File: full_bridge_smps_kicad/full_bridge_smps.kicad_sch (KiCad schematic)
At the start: 0 parts

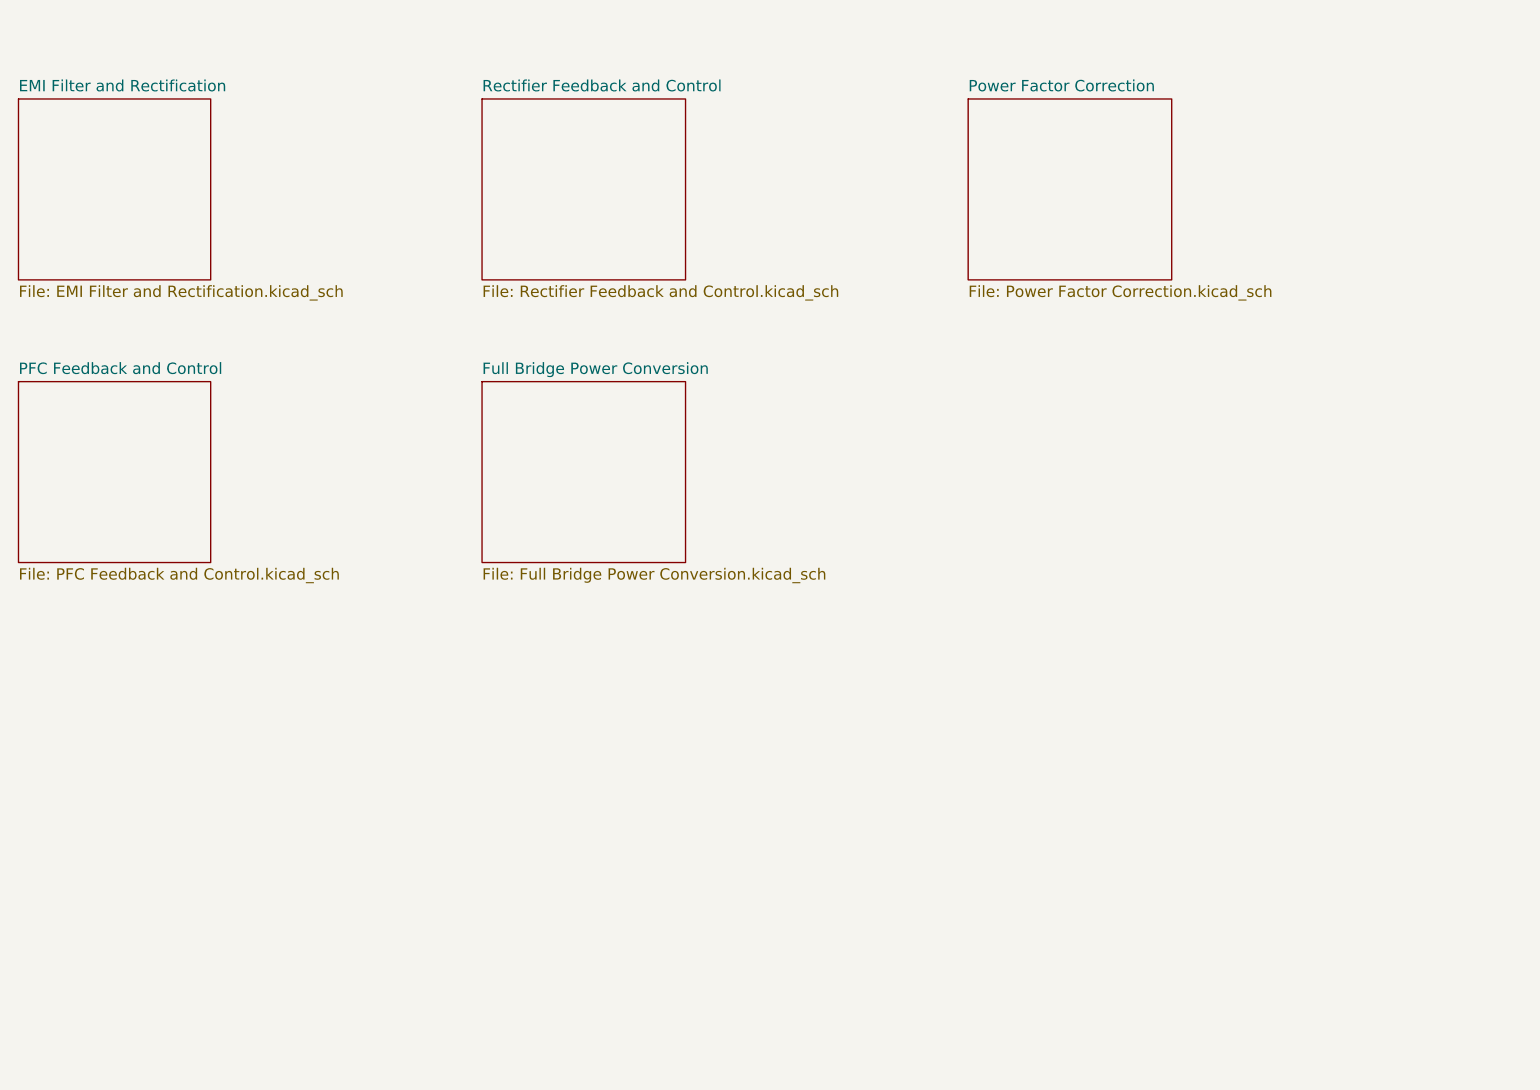
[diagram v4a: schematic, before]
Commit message: Finishing up the output rectification, creating new pages for the corresponding feedback and drive circuits
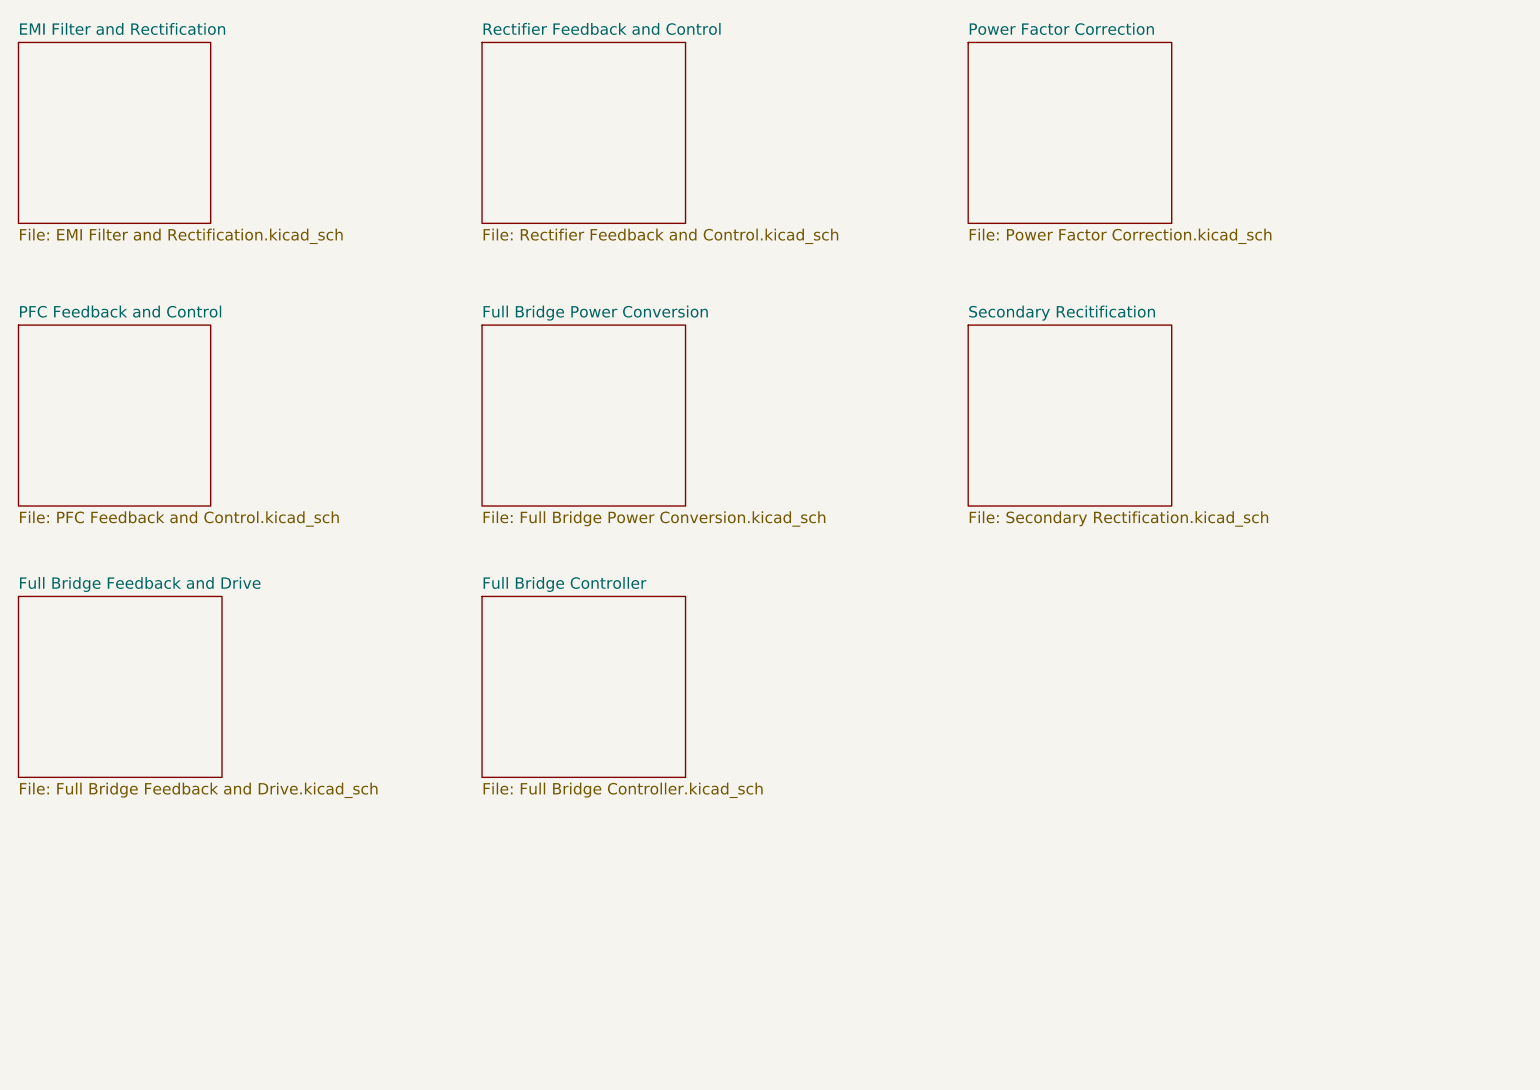
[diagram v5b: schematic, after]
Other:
- added sheet Full Bridge Controller (Full Bridge Controller.kicad_sch)
- added sheet Full Bridge Feedback and Drive (Full Bridge Feedback and Drive.kicad_sch)
- added sheet Secondary Recitification (Secondary Rectification.kicad_sch)
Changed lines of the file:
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@@
     (rev "1.0.0")
   )
-  (sheet (at 24.13 22.86) (size 21.59 20.32) (fields_autoplaced)
+  (sheet (at 24.13 16.51) (size 21.59 20.32) (fields_autoplaced)
     (stroke (width 0.1524) (type solid))
     (fill (color 0 0 0 0.0000))
-    (property "Sheetname" "EMI Filter and Rectification" (at 24.13 22.1484 0)
+    (property "Sheetname" "EMI Filter and Rectification" (at 24.13 15.7984 0)
       (effects (font (size 1.27 1.27)) (justify left bottom))
     )
-    (property "Sheetfile" "EMI Filter and Rectification.kicad_sch" (at 24.13 43.7646 0)
+    (property "Sheetfile" "EMI Filter and Rectification.kicad_sch" (at 24.13 37.4146 0)
       (effects (font (size 1.27 1.27)) (justify left top))
     )
@@
     )
   )
-  (sheet (at 76.2 54.61) (size 22.86 20.32) (fields_autoplaced)
+  (sheet (at 24.13 78.74) (size 22.86 20.32) (fields_autoplaced)
     (stroke (width 0.1524) (type solid))
     (fill (color 0 0 0 0.0000))
-    (property "Sheetname" "Full Bridge Power Conversion" (at 76.2 53.8984 0)
+    (property "Sheetname" "Full Bridge Feedback and Drive" (at 24.13 78.0284 0)
       (effects (font (size 1.27 1.27)) (justify left bottom))
     )
-    (property "Sheetfile" "Full Bridge Power Conversion.kicad_sch" (at 76.2 75.5146 0)
+    (property "Sheetfile" "Full Bridge Feedback and Drive.kicad_sch" (at 24.13 99.6446 0)
+      (effects (font (size 1.27 1.27)) (justify left top))
+    )
+    (instances
+      (project "full_bridge_smps"
+        (path "/f89200e7-8fc9-4acb-bb2b-7da3a53d52f5" (page "8"))
+      )
+    )
+  )
+  (sheet (at 76.2 48.26) (size 22.86 20.32) (fields_autoplaced)
+    (stroke (width 0.1524) (type solid))
+    (fill (color 0 0 0 0.0000))
+    (property "Sheetname" "Full Bridge Power Conversion" (at 76.2 47.5484 0)
+      (effects (font (size 1.27 1.27)) (justify left bottom))
+    )
+    (property "Sheetfile" "Full Bridge Power Conversion.kicad_sch" (at 76.2 69.1646 0)
       (effects (font (size 1.27 1.27)) (justify left top))
     )
@@
     )
   )
-  (sheet (at 130.81 22.86) (size 22.86 20.32) (fields_autoplaced)
+  (sheet (at 76.2 78.74) (size 22.86 20.32) (fields_autoplaced)
     (stroke (width 0.1524) (type solid))
     (fill (color 0 0 0 0.0000))
-    (property "Sheetname" "Power Factor Correction" (at 130.81 22.1484 0)
+    (property "Sheetname" "Full Bridge Controller" (at 76.2 78.0284 0)
       (effects (font (size 1.27 1.27)) (justify left bottom))
     )
-    (property "Sheetfile" "Power Factor Correction.kicad_sch" (at 130.81 43.7646 0)
+    (property "Sheetfile" "Full Bridge Controller.kicad_sch" (at 76.2 99.6446 0)
+      (effects (font (size 1.27 1.27)) (justify left top))
+    )
+    (instances
+      (project "full_bridge_smps"
+        (path "/f89200e7-8fc9-4acb-bb2b-7da3a53d52f5" (page "9"))
+      )
+    )
+  )
+  (sheet (at 130.81 48.26) (size 22.86 20.32) (fields_autoplaced)
+    (stroke (width 0.1524) (type solid))
+    (fill (color 0 0 0 0.0000))
+    (property "Sheetname" "Secondary Recitification" (at 130.81 47.5484 0)
+      (effects (font (size 1.27 1.27)) (justify left bottom))
+    )
+    (property "Sheetfile" "Secondary Rectification.kicad_sch" (at 130.81 69.1646 0)
+      (effects (font (size 1.27 1.27)) (justify left top))
+    )
+    (instances
+      (project "full_bridge_smps"
+        (path "/f89200e7-8fc9-4acb-bb2b-7da3a53d52f5" (page "7"))
+      )
+    )
+  )
+  (sheet (at 130.81 16.51) (size 22.86 20.32) (fields_autoplaced)
+    (stroke (width 0.1524) (type solid))
+    (fill (color 0 0 0 0.0000))
+    (property "Sheetname" "Power Factor Correction" (at 130.81 15.7984 0)
+      (effects (font (size 1.27 1.27)) (justify left bottom))
+    )
+    (property "Sheetfile" "Power Factor Correction.kicad_sch" (at 130.81 37.4146 0)
       (effects (font (size 1.27 1.27)) (justify left top))
     )
@@
     )
   )
-  (sheet (at 76.2 22.86) (size 22.86 20.32) (fields_autoplaced)
+  (sheet (at 76.2 16.51) (size 22.86 20.32) (fields_autoplaced)
     (stroke (width 0.1524) (type solid))
     (fill (color 0 0 0 0.0000))
-    (property "Sheetname" "Rectifier Feedback and Control" (at 76.2 22.1484 0)
+    (property "Sheetname" "Rectifier Feedback and Control" (at 76.2 15.7984 0)
       (effects (font (size 1.27 1.27)) (justify left bottom))
     )
-    (property "Sheetfile" "Rectifier Feedback and Control.kicad_sch" (at 76.2 43.7646 0)
+    (property "Sheetfile" "Rectifier Feedback and Control.kicad_sch" (at 76.2 37.4146 0)
       (effects (font (size 1.27 1.27)) (justify left top))
     )
@@
     )
   )
-  (sheet (at 24.13 54.61) (size 21.59 20.32) (fields_autoplaced)
+  (sheet (at 24.13 48.26) (size 21.59 20.32) (fields_autoplaced)
     (stroke (width 0.1524) (type solid))
     (fill (color 0 0 0 0.0000))
-    (property "Sheetname" "PFC Feedback and Control" (at 24.13 53.8984 0)
+    (property "Sheetname" "PFC Feedback and Control" (at 24.13 47.5484 0)
       (effects (font (size 1.27 1.27)) (justify left bottom))
     )
-    (property "Sheetfile" "PFC Feedback and Control.kicad_sch" (at 24.13 75.5146 0)
+    (property "Sheetfile" "PFC Feedback and Control.kicad_sch" (at 24.13 69.1646 0)
       (effects (font (size 1.27 1.27)) (justify left top))
     )

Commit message: A bit of refactoring, saving work for the day
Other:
- removed sheet Full Bridge Feedback and Drive
- added sheet Full Bridge Current Feedback and Drive (Full Bridge Current Feedback and Drive.kicad_sch)
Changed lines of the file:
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@@
     (rev "1.0.0")
+  )
+  (sheet (at 24.13 77.47) (size 22.86 20.32) (fields_autoplaced)
+    (stroke (width 0.1524) (type solid))
+    (fill (color 0 0 0 0.0000))
+    (property "Sheetname" "Full Bridge Current Feedback and Drive" (at 24.13 76.7584 0)
+      (effects (font (size 1.27 1.27)) (justify left bottom))
+    )
+    (property "Sheetfile" "Full Bridge Current Feedback and Drive.kicad_sch" (at 24.13 98.3746 0)
+      (effects (font (size 1.27 1.27)) (justify left top))
+    )
+    (instances
+      (project "full_bridge_smps"
+        (path "/f89200e7-8fc9-4acb-bb2b-7da3a53d52f5" (page "8"))
+      )
+    )
   )
   (sheet (at 24.13 16.51) (size 21.59 20.32) (fields_autoplaced)
@@
     )
   )
-  (sheet (at 24.13 78.74) (size 22.86 20.32) (fields_autoplaced)
+  (sheet (at 85.09 46.99) (size 22.86 20.32) (fields_autoplaced)
     (stroke (width 0.1524) (type solid))
     (fill (color 0 0 0 0.0000))
-    (property "Sheetname" "Full Bridge Feedback and Drive" (at 24.13 78.0284 0)
+    (property "Sheetname" "Full Bridge Power Conversion" (at 85.09 46.2784 0)
       (effects (font (size 1.27 1.27)) (justify left bottom))
     )
-    (property "Sheetfile" "Full Bridge Feedback and Drive.kicad_sch" (at 24.13 99.6446 0)
-      (effects (font (size 1.27 1.27)) (justify left top))
-    )
-    (instances
-      (project "full_bridge_smps"
-        (path "/f89200e7-8fc9-4acb-bb2b-7da3a53d52f5" (page "8"))
-      )
-    )
-  )
-  (sheet (at 76.2 48.26) (size 22.86 20.32) (fields_autoplaced)
-    (stroke (width 0.1524) (type solid))
-    (fill (color 0 0 0 0.0000))
-    (property "Sheetname" "Full Bridge Power Conversion" (at 76.2 47.5484 0)
-      (effects (font (size 1.27 1.27)) (justify left bottom))
-    )
-    (property "Sheetfile" "Full Bridge Power Conversion.kicad_sch" (at 76.2 69.1646 0)
+    (property "Sheetfile" "Full Bridge Power Conversion.kicad_sch" (at 85.09 67.8946 0)
       (effects (font (size 1.27 1.27)) (justify left top))
     )
@@
     )
   )
-  (sheet (at 76.2 78.74) (size 22.86 20.32) (fields_autoplaced)
+  (sheet (at 85.09 77.47) (size 22.86 20.32) (fields_autoplaced)
     (stroke (width 0.1524) (type solid))
     (fill (color 0 0 0 0.0000))
-    (property "Sheetname" "Full Bridge Controller" (at 76.2 78.0284 0)
+    (property "Sheetname" "Full Bridge Controller" (at 85.09 76.7584 0)
       (effects (font (size 1.27 1.27)) (justify left bottom))
     )
-    (property "Sheetfile" "Full Bridge Controller.kicad_sch" (at 76.2 99.6446 0)
+    (property "Sheetfile" "Full Bridge Controller.kicad_sch" (at 85.09 98.3746 0)
       (effects (font (size 1.27 1.27)) (justify left top))
     )
@@
     )
   )
-  (sheet (at 130.81 48.26) (size 22.86 20.32) (fields_autoplaced)
+  (sheet (at 146.05 46.99) (size 22.86 20.32) (fields_autoplaced)
     (stroke (width 0.1524) (type solid))
     (fill (color 0 0 0 0.0000))
-    (property "Sheetname" "Secondary Recitification" (at 130.81 47.5484 0)
+    (property "Sheetname" "Secondary Recitification" (at 146.05 46.2784 0)
       (effects (font (size 1.27 1.27)) (justify left bottom))
     )
-    (property "Sheetfile" "Secondary Rectification.kicad_sch" (at 130.81 69.1646 0)
+    (property "Sheetfile" "Secondary Rectification.kicad_sch" (at 146.05 67.8946 0)
       (effects (font (size 1.27 1.27)) (justify left top))
     )
@@
     )
   )
-  (sheet (at 130.81 16.51) (size 22.86 20.32) (fields_autoplaced)
+  (sheet (at 146.05 16.51) (size 22.86 20.32) (fields_autoplaced)
     (stroke (width 0.1524) (type solid))
     (fill (color 0 0 0 0.0000))
-    (property "Sheetname" "Power Factor Correction" (at 130.81 15.7984 0)
+    (property "Sheetname" "Power Factor Correction" (at 146.05 15.7984 0)
       (effects (font (size 1.27 1.27)) (justify left bottom))
     )
-    (property "Sheetfile" "Power Factor Correction.kicad_sch" (at 130.81 37.4146 0)
+    (property "Sheetfile" "Power Factor Correction.kicad_sch" (at 146.05 37.4146 0)
       (effects (font (size 1.27 1.27)) (justify left top))
     )
@@
     )
   )
-  (sheet (at 76.2 16.51) (size 22.86 20.32) (fields_autoplaced)
+  (sheet (at 85.09 16.51) (size 22.86 20.32) (fields_autoplaced)
     (stroke (width 0.1524) (type solid))
     (fill (color 0 0 0 0.0000))
-    (property "Sheetname" "Rectifier Feedback and Control" (at 76.2 15.7984 0)
+    (property "Sheetname" "Rectifier Feedback and Control" (at 85.09 15.7984 0)
       (effects (font (size 1.27 1.27)) (justify left bottom))
     )
-    (property "Sheetfile" "Rectifier Feedback and Control.kicad_sch" (at 76.2 37.4146 0)
+    (property "Sheetfile" "Rectifier Feedback and Control.kicad_sch" (at 85.09 37.4146 0)
       (effects (font (size 1.27 1.27)) (justify left top))
     )
@@
     )
   )
-  (sheet (at 24.13 48.26) (size 21.59 20.32) (fields_autoplaced)
+  (sheet (at 24.13 46.99) (size 21.59 20.32) (fields_autoplaced)
     (stroke (width 0.1524) (type solid))
     (fill (color 0 0 0 0.0000))
-    (property "Sheetname" "PFC Feedback and Control" (at 24.13 47.5484 0)
+    (property "Sheetname" "PFC Feedback and Control" (at 24.13 46.2784 0)
       (effects (font (size 1.27 1.27)) (justify left bottom))
     )
-    (property "Sheetfile" "PFC Feedback and Control.kicad_sch" (at 24.13 69.1646 0)
+    (property "Sheetfile" "PFC Feedback and Control.kicad_sch" (at 24.13 67.8946 0)
       (effects (font (size 1.27 1.27)) (justify left top))
     )
